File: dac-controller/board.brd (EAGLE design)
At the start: 100 x 100 mm, 39 parts, among them IC1 LM317MABT, IC2 ISO7220C, IC3 74HCT595D

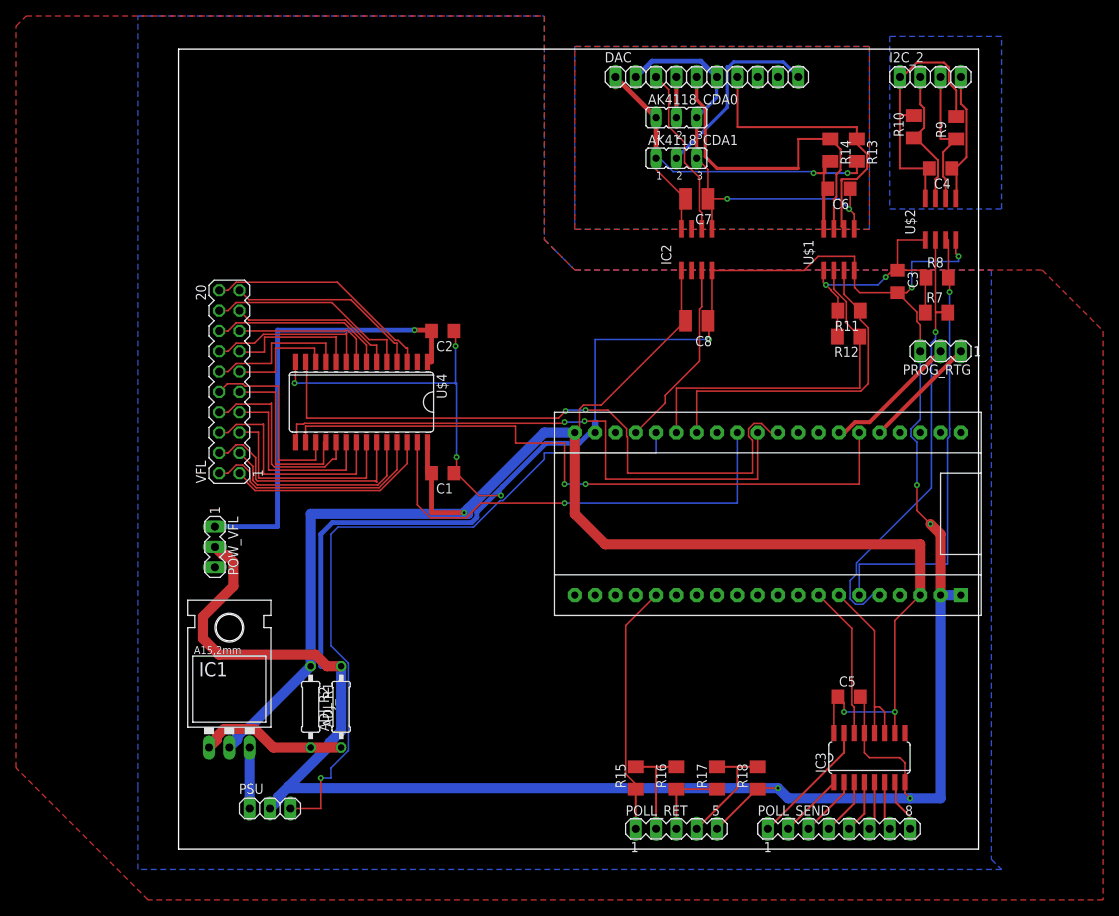
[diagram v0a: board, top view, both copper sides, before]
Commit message: added dc-ac convert, added correct connector(s) for VFD, ripped up some traces to move things around
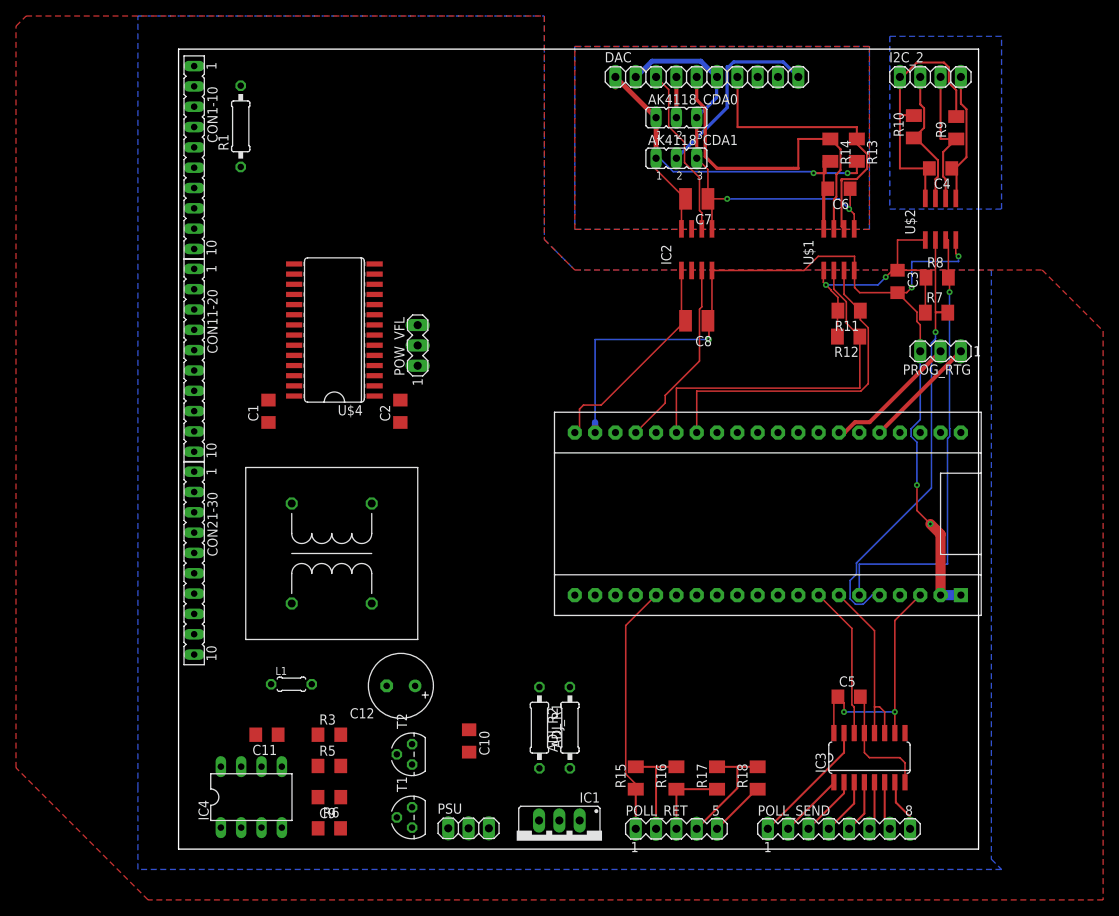
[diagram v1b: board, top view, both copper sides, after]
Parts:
- removed VFL: (no value), con-lstb:MA10-2
- added C10, C9: 0.1uF, rcl:C1206
- added C11: 0.01uF, rcl:C1206
- added C12: 2700uF, rcl:E3,5-8
- added CON1-10, CON11-20, CON21-30: (no value), con-lsta:FE10
- added IC4: NE555, st-microelectronics:DIL-08
- added L1: (no value), rcl:0204/5
- added R1: 100R, rcl:0207/10
- added R3: 10k, rcl:R1206
- added R5: 125k, rcl:R1206
- added R6: 100, rcl:R1206
- added T1, T2: (no value), transistor:TO92
- added U$5: TRAFO-1:1, archi_laptop:TRAFO-10-12.5
- IC1: value LM317MABT -> (none); device v-reg:TO220L1 -> v-reg:317TS
- moved IC1 44.1 mm to (47.6, 1.04), turned to 180 degrees
- moved POW_VFL 35.7 mm to (29.9, 63.0), turned to 90 degrees
- moved ADJ_R2 28.7 mm to (48.9, 15.2)
- moved ADJ_R1 28.7 mm to (45.1, 15.2)
- moved PSU 24.9 mm to (36.2, 2.60)
- moved C1 23.1 mm to (11.2, 54.7), turned to 90 degrees
- moved C2 11.4 mm to (27.7, 54.7), turned to 90 degrees
- moved U$4 9.62 mm to (19.5, 64.9), turned to 90 degrees
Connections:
- new net N$11: CON11-20.7, U$4.21
- new net N$12: CON21-30.10, U$4.5
- new net N$13: CON21-30.9, U$4.6
- new net N$49: R6.1, T1.2, T2.2
- new net N$54: C12.-, L1.2
- new net N$7: CON1-10.2, R1.2
- new net N$8: CON11-20.1, U$5.P$1
- new net N$9: CON11-20.2, U$5.P$2
- net 5V_RAW: now also C10.1, IC4.4, IC4.8, R1.1, R3.2, T1.3
- net GND: now also C10.2, C11.2, C9.2, CON1-10.1, CON21-30.6, IC4.1, T2.3, U$5.P$3
- net N$19: now also CON21-30.8, U$4.7; no longer U$4.26, VFL.1
- net N$20: now also CON21-30.7, U$4.8; no longer U$4.25, VFL.2
- net N$21: now also CON21-30.5, U$4.9; no longer U$4.24, VFL.3
- net N$22: now also CON21-30.4, U$4.10; no longer U$4.23, VFL.4
- net N$23: now also CON21-30.3, U$4.11; no longer U$4.22, VFL.5
- net N$31: now also CON21-30.2, U$4.12; no longer U$4.20, VFL.7
- net N$32: now also CON21-30.1, U$4.17; no longer U$4.18, VFL.9
- net N$33: now also CON11-20.10, U$4.18; no longer U$4.12, VFL.11
- net N$34: now also CON11-20.9, U$4.19; no longer U$4.10, VFL.13
- net N$35: now also CON11-20.8, U$4.20; no longer U$4.8, VFL.15
- net N$36: now also CON11-20.6, U$4.22; no longer U$4.6, VFL.17
- net N$37: now also CON11-20.5, U$4.23; no longer U$4.4, VFL.19
- net N$38: now also CON11-20.4, U$4.24; no longer U$4.21, VFL.6
- net N$39: now also CON11-20.3, U$4.25; no longer U$4.19, VFL.8
- net N$40: now also C11.1, IC4.5; no longer U$4.17, VFL.10
- net N$41: now also IC4.7, R3.1, R5.2; no longer U$4.11, VFL.12
- net N$42: now also C9.1, IC4.2, IC4.6, R5.1; no longer U$4.9, VFL.14
- net N$43: now also IC4.3, R6.2; no longer U$4.7, VFL.16
- net N$44: now also C12.+, T1.1, T2.1; no longer U$4.5, VFL.18
- net N$45: now also L1.1, U$5.P$4; no longer U$4.3, VFL.20
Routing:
- net GND: track 418.6 -> 143.2 mm, vias 11 -> 5
- net VCC: track 242.6 -> 95.2 mm, vias 5 -> 4
- net RELAY_CTRL: track 89.0 -> 0.00 mm, vias 1 -> 0
- net N$17: track 85.3 -> 0.00 mm, vias 2 -> 0
- net N$18: track 80.0 -> 0.00 mm, vias 2 -> 0
- net N$2: track 73.4 -> 0.00 mm, vias 2 -> 0
- net N$16: track 58.2 -> 0.00 mm, vias 1 -> 0
- net N$24: track 56.1 -> 0.00 mm, vias 1 -> 0
- net N$45: track 29.1 -> 0.00 mm
- net N$20: track 28.9 -> 0.00 mm
- net N$22: track 28.6 -> 0.00 mm
- net N$38: track 27.8 -> 0.00 mm
- net N$23: track 26.2 -> 0.00 mm
- net N$44: track 26.1 -> 0.00 mm
- net N$19: track 26.0 -> 0.00 mm
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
